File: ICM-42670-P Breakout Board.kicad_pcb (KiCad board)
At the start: 2 copper layers, 18 x 26.5 mm, 12 parts, among them J2 Conn_01x09_Pin, U1 ICM-42670-P, U2 MCP1700x-330xxTT

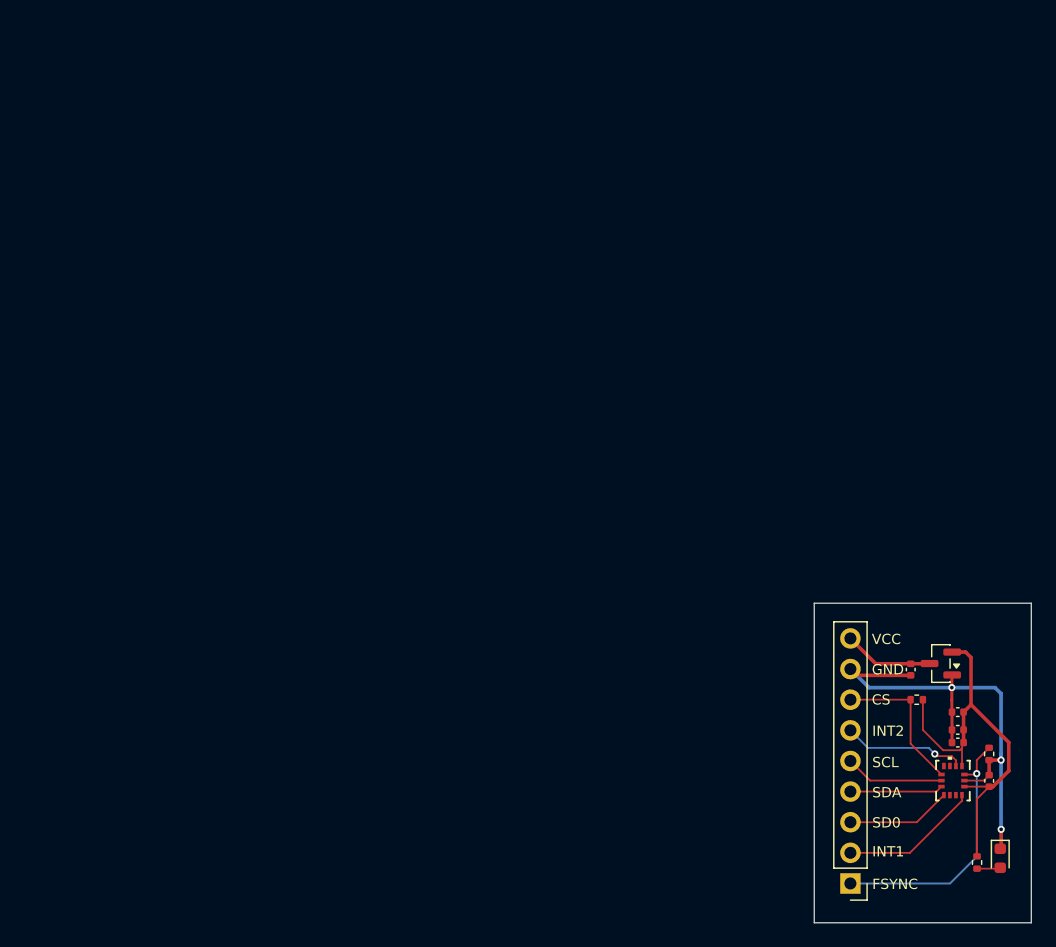
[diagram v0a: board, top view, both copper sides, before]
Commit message: Changed BOM
Bom Reflects General Parts now
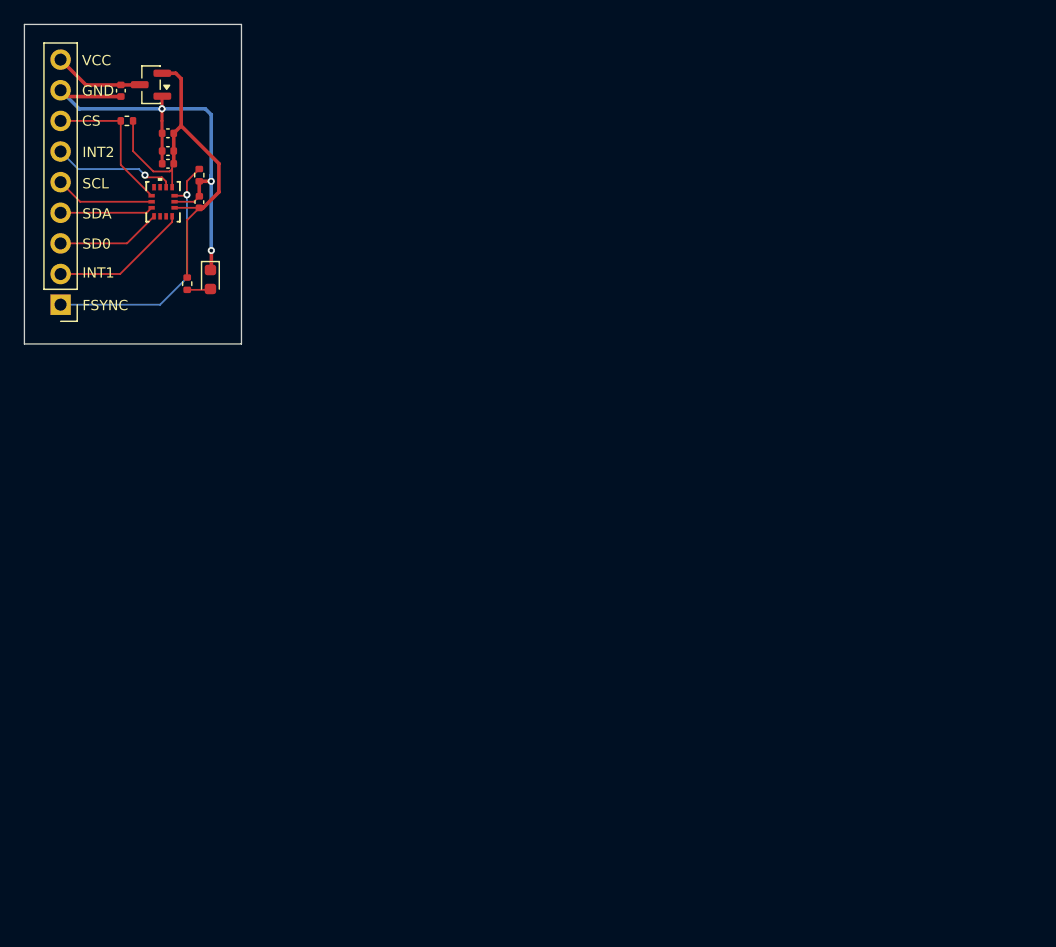
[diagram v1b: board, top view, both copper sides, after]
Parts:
- moved C2 81.2 mm to (67.4, 34.6)
- moved D1 81.2 mm to (70.9, 44.1)
- moved C1 81.2 mm to (67.4, 33.5)
- moved C3 81.2 mm to (70.0, 37.7)
- moved C4 81.2 mm to (67.4, 32.0)
- moved C5 81.2 mm to (63.5, 28.5)
- moved R1 81.2 mm to (64.0, 31.0)
- moved R2 81.2 mm to (70.0, 35.5)
- moved R3 81.2 mm to (69.0, 44.5)
- moved U1 81.2 mm to (67.0, 37.7)
- moved U2 81.2 mm to (66.0, 28.0)
- moved J2 81.2 mm to (58.5, 46.2)
